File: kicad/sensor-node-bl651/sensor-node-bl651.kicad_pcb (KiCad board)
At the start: 2 copper layers, 18.2 x 54.5 mm, 30 parts, among them T1 TPS6031x, U1 DMP2008UFG-7, U2 DMP2008UFG-7, U3 LSM303AGR, Y1 32.768 kHz

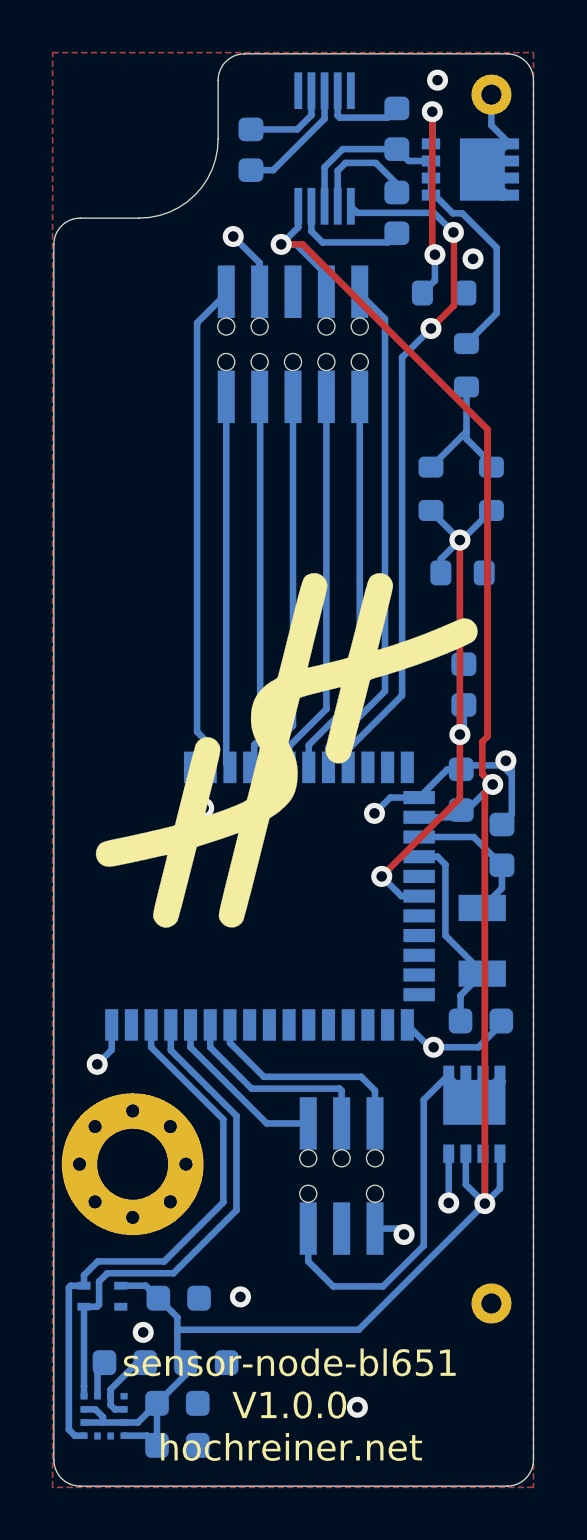
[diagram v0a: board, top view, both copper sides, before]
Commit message: add more sensors
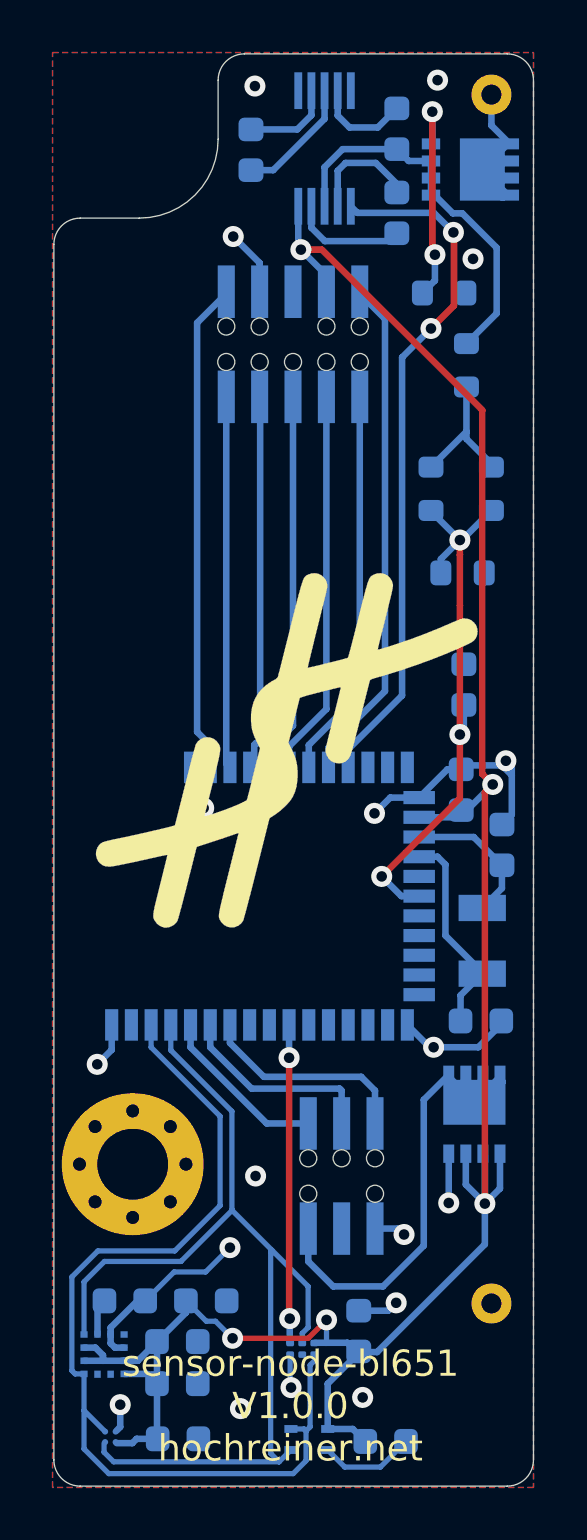
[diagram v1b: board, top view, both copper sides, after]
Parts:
- added C11: 1µF 0603, Capacitor_SMD:C_0603_1608Metric, B.Cu at (151.8, 121.3)
- added C6: 2.2µF 0603, Capacitor_SMD:C_0603_1608Metric, B.Cu at (145.0, 125.5)
- added M1: MMC5603NJ, HH_Memsic:MMC5603NJ, B.Cu at (142.4, 125.4)
- added M2: MXC4005XC, HH_Memsic:MXC400xXC, B.Cu at (149.7, 122.0)
- moved C1 9.58 mm to (152.9, 125.5)
- moved S1 9.58 mm to (150.0, 125.5)
- moved C8 2.35 mm to (144.9, 123.3)
- moved C10 2.35 mm to (146.1, 120.2)
- moved C7 2.35 mm to (142.9, 120.2)
- moved C9 2.35 mm to (144.9, 121.8)
- moved U3 2.35 mm to (142.2, 122.2)
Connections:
- BL1 pad 10: (no net) -> /mcu/INT_M_XL
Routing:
- net /sensors/SDA: track 19.3 -> 39.1 mm
- net /sensors/SCL: track 21.4 -> 36.6 mm
- net /mcu/INT_M_XL: track 0.00 -> 12.1 mm, vias 0 -> 2
- net GND: track 28.7 -> 40.5 mm, vias 13 -> 18
- net /mcu/VDD: track 82.1 -> 88.5 mm, vias 3 -> 5
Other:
- net class I2C added: clearance 0.2, trace_width 0.2, via_dia 0.8, via_drill 0.4

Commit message: add pull down on snooze line
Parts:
- added R3: 100k 0603, Resistor_SMD:R_0603_1608Metric, B.Cu at (155.8, 94.3)
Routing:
- net /mcu/~SNOOZE: track 26.3 -> 27.8 mm

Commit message: update version number
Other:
- board text added: "sensor-node-bl651 V1.1.0 hochreiner.net"
- board text removed: "sensor-node-bl651 V1.0.0 hochreiner.net"

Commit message: clean up
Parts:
- moved U1 0.40 mm to (156.2, 113.5)
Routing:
- net /mcu/VDD: track 88.5 -> 87.3 mm
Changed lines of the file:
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@@
     (thickness 1.6)
     (drawings 13)
-    (tracks 321)
+    (tracks 326)
     (zones 0)
     (modules 35)
@@
     (tags capacitor)
     (attr smd)
-    (fp_text reference C4 (at 2.575 -0.425 90) (layer B.SilkS)
+    (fp_text reference C4 (at 2.225 0.2 90) (layer B.SilkS)
       (effects (font (size 1 1) (thickness 0.15)) (justify mirror))
     )
@@
     (tags capacitor)
     (attr smd)
-    (fp_text reference C2 (at 2.125 0.05) (layer B.SilkS)
+    (fp_text reference C2 (at 1.825 -0.025) (layer B.SilkS)
       (effects (font (size 1 1) (thickness 0.15)) (justify mirror))
     )
@@
     (tags resistor)
     (attr smd)
-    (fp_text reference R6 (at 2.45 0) (layer B.SilkS)
+    (fp_text reference R6 (at 2.15 0 90) (layer B.SilkS)
       (effects (font (size 1 1) (thickness 0.15)) (justify mirror))
     )
@@
   )
   (module HH_DiodesIncorporated:DMP2008UFG-7 (layer B.Cu)
-    (at 156.25 113.1 180)
-    (fp_text reference U1 (at -1.35 -2.75) (layer B.SilkS)
+    (at 156.25 113.5 180)
+    (fp_text reference U1 (at 0 -3.975) (layer B.SilkS)
       (effects (font (size 1 1) (thickness 0.15)) (justify mirror))
     )
@@
     (tags resistor)
     (attr smd)
-    (fp_text reference R4 (at 0 1.43 90) (layer B.SilkS)
+    (fp_text reference R4 (at 0 1.325 90) (layer B.SilkS)
       (effects (font (size 1 1) (thickness 0.15)) (justify mirror))
     )
@@
     (tags capacitor)
     (attr smd)
-    (fp_text reference C15 (at 2.85 0.25 90) (layer B.SilkS)
+    (fp_text reference C15 (at 2.85 -0.1 90) (layer B.SilkS)
       (effects (font (size 1 1) (thickness 0.15)) (justify mirror))
     )
@@
   (segment (start 148.08 80.705) (end 147.075 79.7) (width 0.25) (layer B.Cu) (net 1))
   (via (at 155.275 116.475) (size 0.8) (drill 0.4) (layers F.Cu B.Cu) (net 1))
-  (segment (start 155.275 114.6) (end 155.275 116.475) (width 0.25) (layer B.Cu) (net 1))
   (via (at 153.575 117.675) (size 0.8) (drill 0.4) (layers F.Cu B.Cu) (net 1))
   (segment (start 153.35 117.45) (end 153.575 117.675) (width 0.25) (layer B.Cu) (net 1))
@@
   (segment (start 151.5 75.55) (end 152.575 75.55) (width 0.25) (layer B.Cu) (net 1))
   (segment (start 151.05 74.15) (end 151.05 75.1) (width 0.25) (layer B.Cu) (net 1))
+  (segment (start 155.275 115.025) (end 155.275 116.475) (width 0.25) (layer B.Cu) (net 1))
   (segment (start 141.3975 124.3725) (end 142.159999 125.134999) (width 0.2) (layer B.Cu) (net 2))
   (segment (start 141.3975 122.98) (end 141.3975 124.3725) (width 0.2) (layer B.Cu) (net 2))
@@
   (segment (start 142.12 122.27) (end 141.83 121.98) (width 0.25) (layer B.Cu) (net 11))
   (via (at 156.65 116.5) (size 0.8) (drill 0.4) (layers F.Cu B.Cu) (net 11))
-  (segment (start 156.65 114.675) (end 156.575 114.6) (width 0.25) (layer B.Cu) (net 11))
-  (segment (start 156.65 116.5) (end 156.65 114.675) (width 0.25) (layer B.Cu) (net 11))
-  (segment (start 157.225 115.925) (end 156.65 116.5) (width 0.25) (layer B.Cu) (net 11))
-  (segment (start 157.225 114.6) (end 157.225 115.925) (width 0.25) (layer B.Cu) (net 11))
-  (segment (start 155.925 115.775) (end 156.65 116.5) (width 0.25) (layer B.Cu) (net 11))
-  (segment (start 155.925 114.6) (end 155.925 115.775) (width 0.25) (layer B.Cu) (net 11))
   (segment (start 155.475 101.8) (end 155.75 101.525) (width 0.25) (layer B.Cu) (net 11))
   (segment (start 154.15 101.8) (end 155.475 101.8) (width 0.25) (layer B.Cu) (net 11))
@@
   (segment (start 149.55 78.55) (end 149.55 80.1) (width 0.25) (layer B.Cu) (net 11))
   (via (at 149.65 80.2) (size 0.8) (drill 0.4) (layers F.Cu B.Cu) (net 11))
+  (segment (start 155.925 115.775) (end 156.65 116.5) (width 0.25) (layer B.Cu) (net 11))
+  (segment (start 155.925 115) (end 155.925 115.775) (width 0.25) (layer B.Cu) (net 11))
+  (segment (start 156.575 116.425) (end 156.65 116.5) (width 0.25) (layer B.Cu) (net 11))
+  (segment (start 156.575 115) (end 156.575 116.425) (width 0.25) (layer B.Cu) (net 11))
+  (segment (start 157.225 115.925) (end 156.65 116.5) (width 0.25) (layer B.Cu) (net 11))
+  (segment (start 157.225 115) (end 157.225 115.925) (width 0.25) (layer B.Cu) (net 11))
   (segment (start 148.35 113.45) (end 149.93 113.45) (width 0.25) (layer B.Cu) (net 12))
   (segment (start 145.45 110.55) (end 148.35 113.45) (width 0.25) (layer B.Cu) (net 12))
@@
   (segment (start 141.91 121.4675) (end 141.91 120.465) (width 0.25) (layer B.Cu) (net 18))
   (segment (start 156.575 112.32) (end 156.25 112.645) (width 0.25) (layer B.Cu) (net 19))
-  (segment (start 156.575 111.6) (end 156.575 112.32) (width 0.25) (layer B.Cu) (net 19))
-  (segment (start 157.225 111.67) (end 156.25 112.645) (width 0.25) (layer B.Cu) (net 19))
-  (segment (start 157.225 111.6) (end 157.225 111.67) (width 0.25) (layer B.Cu) (net 19))
   (segment (start 155.925 112.32) (end 156.25 112.645) (width 0.25) (layer B.Cu) (net 19))
-  (segment (start 155.925 111.6) (end 155.925 112.32) (width 0.25) (layer B.Cu) (net 19))
-  (segment (start 155.275 111.67) (end 156.25 112.645) (width 0.25) (layer B.Cu) (net 19))
-  (segment (start 155.275 111.6) (end 155.275 111.67) (width 0.25) (layer B.Cu) (net 19))
-  (segment (start 150.88 119.65) (end 149.93 118.7) (width 0.25) (layer B.Cu) (net 19))
-  (segment (start 152.775 119.65) (end 150.88 119.65) (width 0.25) (layer B.Cu) (net 19))
-  (segment (start 149.93 118.7) (end 149.93 117.45) (width 0.25) (layer B.Cu) (net 19))
-  (segment (start 154.325 118.1) (end 152.775 119.65) (width 0.25) (layer B.Cu) (net 19))
-  (segment (start 154.325 112.55) (end 154.325 118.1) (width 0.25) (layer B.Cu) (net 19))
-  (segment (start 155.275 111.6) (end 154.325 112.55) (width 0.25) (layer B.Cu) (net 19))
+  (segment (start 155.95 112.025) (end 155.925 112) (width 0.25) (layer B.Cu) (net 19))
+  (segment (start 155.95 112.725) (end 155.95 112.025) (width 0.25) (layer B.Cu) (net 19))
+  (segment (start 156.25 113.025) (end 155.95 112.725) (width 0.25) (layer B.Cu) (net 19))
+  (segment (start 156.25 113.045) (end 156.25 113.025) (width 0.25) (layer B.Cu) (net 19))
+  (segment (start 156.575 112.72) (end 156.25 113.045) (width 0.25) (layer B.Cu) (net 19))
+  (segment (start 156.575 112) (end 156.575 112.72) (width 0.25) (layer B.Cu) (net 19))
+  (segment (start 157.225 112.4) (end 156.85 112.775) (width 0.25) (layer B.Cu) (net 19))
+  (segment (start 157.225 112) (end 157.225 112.4) (width 0.25) (layer B.Cu) (net 19))
+  (segment (start 155.275 112.325) (end 155.7 112.75) (width 0.25) (layer B.Cu) (net 19))
+  (segment (start 155.275 112) (end 155.275 112.325) (width 0.25) (layer B.Cu) (net 19))
+  (segment (start 154.775 111.975) (end 155.275 111.975) (width 0.25) (layer B.Cu) (net 19))
+  (segment (start 154.325 112.425) (end 154.775 111.975) (width 0.25) (layer B.Cu) (net 19))
+  (segment (start 150.88 119.65) (end 152.775 119.65) (width 0.25) (layer B.Cu) (net 19))
+  (segment (start 154.325 118.1) (end 154.325 112.425) (width 0.25) (layer B.Cu) (net 19))
+  (segment (start 152.775 119.65) (end 154.325 118.1) (width 0.25) (layer B.Cu) (net 19))
+  (segment (start 149.93 118.7) (end 150.88 119.65) (width 0.25) (layer B.Cu) (net 19))
+  (segment (start 149.93 117.45) (end 149.93 118.7) (width 0.25) (layer B.Cu) (net 19))
   (segment (start 148.1 85.745) (end 148.08 85.725) (width 0.25) (layer B.Cu) (net 20))
   (segment (start 148.053589 98.974999) (end 148.1 98.928588) (width 0.25) (layer B.Cu) (net 20))
